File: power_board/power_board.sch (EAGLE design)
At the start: 25 parts, among them K2 RELAY-SPDT, Q1 600mA/40V, U2 ATSAMD21G-A

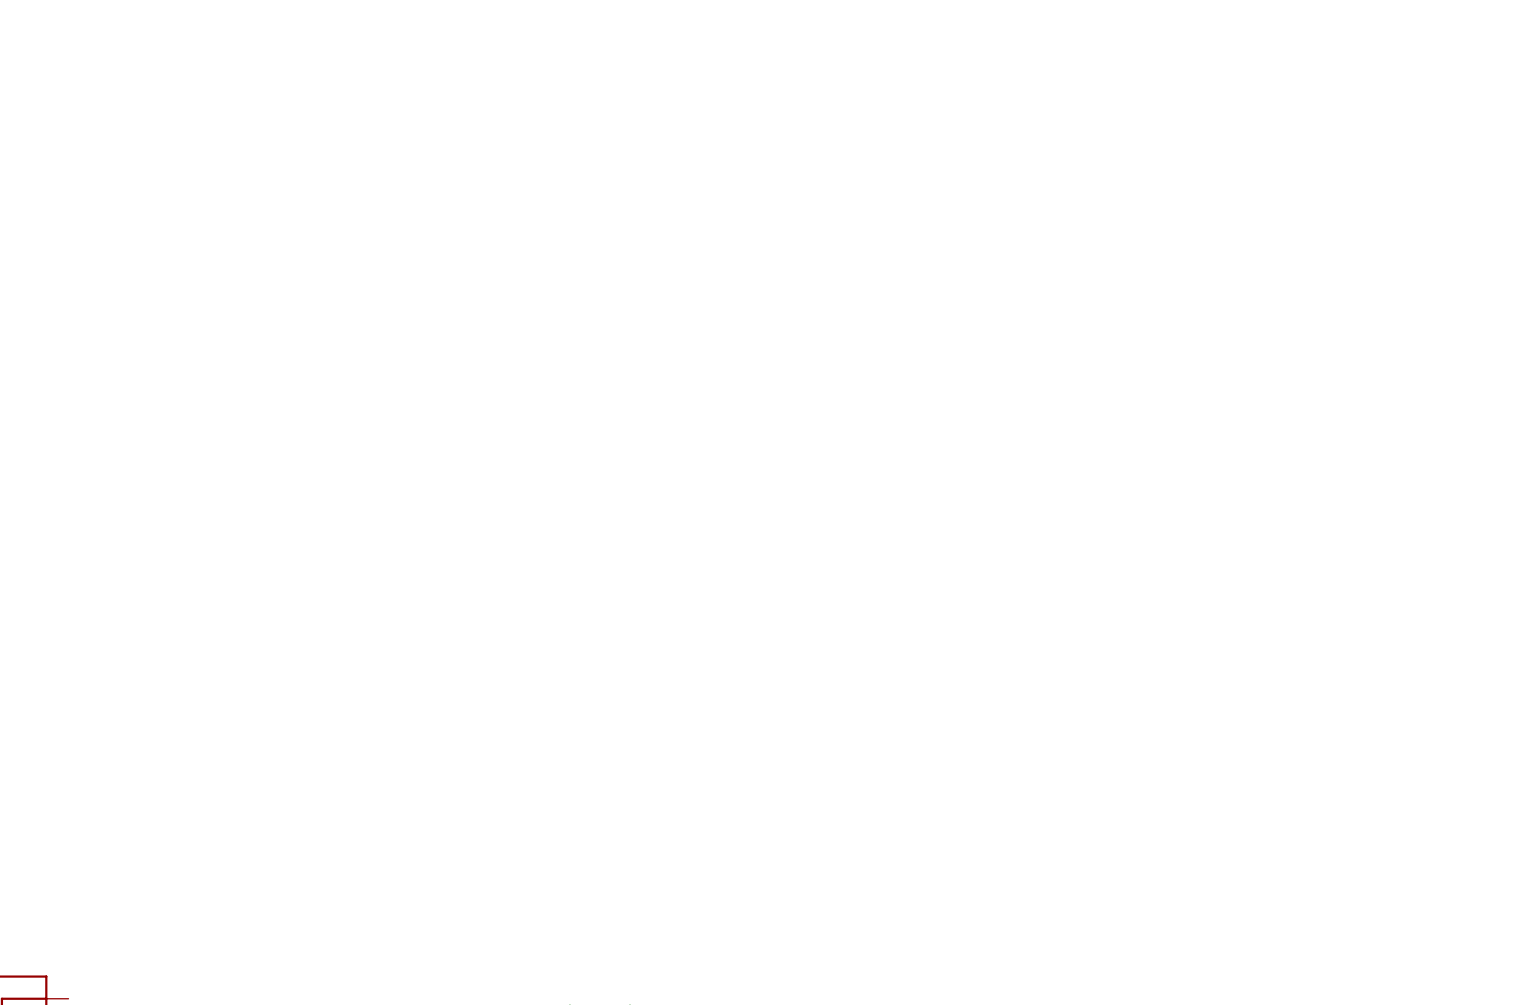
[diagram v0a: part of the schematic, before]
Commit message: Started adding NINA-B1
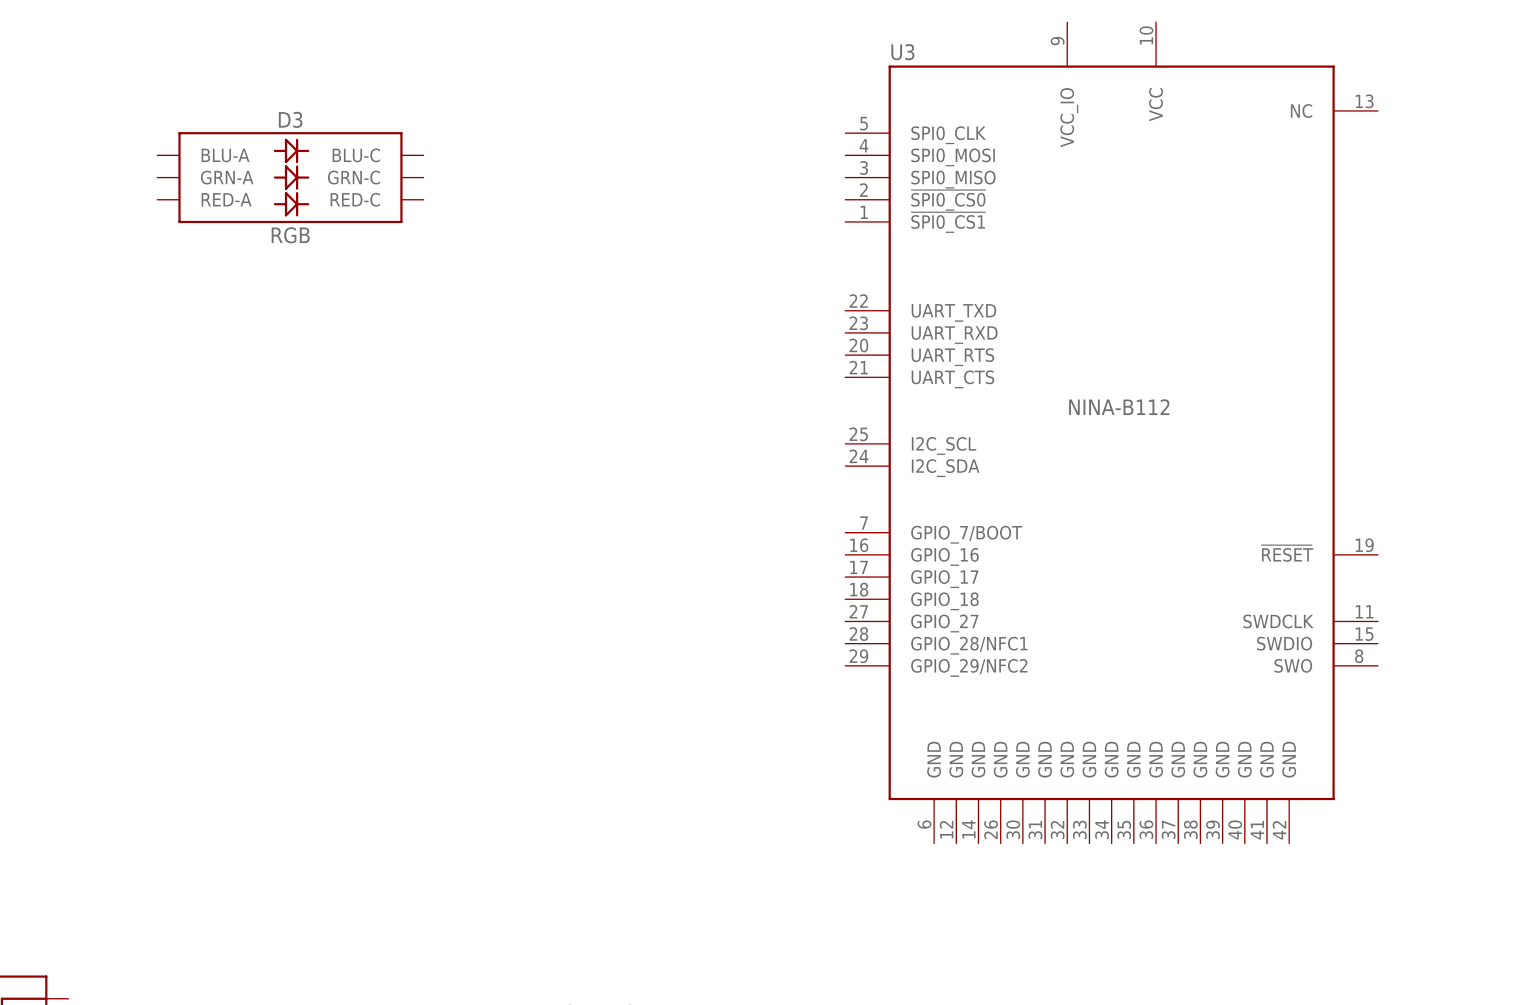
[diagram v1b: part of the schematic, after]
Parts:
- added D3: RGB, SparkFun-LED:LED-RGBPLCC-6
- added U3: NINA-B112, ubloxLib:NINA-B112
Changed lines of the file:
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@@
 <layer number="132" name="bAdjust" color="7" fill="1" visible="yes" active="yes"/>
 <layer number="144" name="Drill_legend" color="7" fill="1" visible="yes" active="yes"/>
+<layer number="145" name="DrillLegend_01-02" color="7" fill="1" visible="yes" active="yes"/>
+<layer number="146" name="DrillLegend_01-15" color="7" fill="1" visible="yes" active="yes"/>
+<layer number="147" name="DrillLegend_01-16" color="7" fill="1" visible="yes" active="yes"/>
+<layer number="148" name="DrillLegend_01-20" color="7" fill="1" visible="yes" active="yes"/>
+<layer number="149" name="DrillLegend_02-15" color="7" fill="1" visible="yes" active="yes"/>
 <layer number="150" name="Notes" color="7" fill="1" visible="yes" active="yes"/>
 <layer number="151" name="HeatSink" color="7" fill="1" visible="yes" active="yes"/>
@@
 <part name="C8" library="SparkFun-Capacitors" deviceset="0.1UF" device="-0603-25V-(+80/-20%)" value="0.1uF"/>
 <part name="U2" library="SparkFun-IC-Microcontroller" deviceset="ATSAMD21G" device="-A"/>
+<part name="U3" library="ubloxLib" deviceset="NINA-B112" device=""/>
+<part name="D3" library="SparkFun-LED" deviceset="LED-RGB" device="PLCC-6" value="RGB"/>
 </parts>
 <sheets>
@@
 <attribute name="VALUE" x="241.3" y="101.346" size="1.778" layer="96" align="top-left"/>
 </instance>
+<instance part="U3" gate="G$1" x="175.26" y="142.24" smashed="yes">
+<attribute name="VALUE" x="170.18" y="144.78" size="1.778" layer="96" align="top-left"/>
+<attribute name="NAME" x="149.86" y="185.42" size="1.778" layer="95" align="top-left"/>
+</instance>
+<instance part="D3" gate="G$1" x="81.28" y="170.18" smashed="yes">
+<attribute name="NAME" x="81.28" y="175.895" size="1.778" layer="95" font="vector" align="bottom-center"/>
+<attribute name="VALUE" x="81.28" y="164.465" size="1.778" layer="95" font="vector" align="top-center"/>
+</instance>
 </instances>

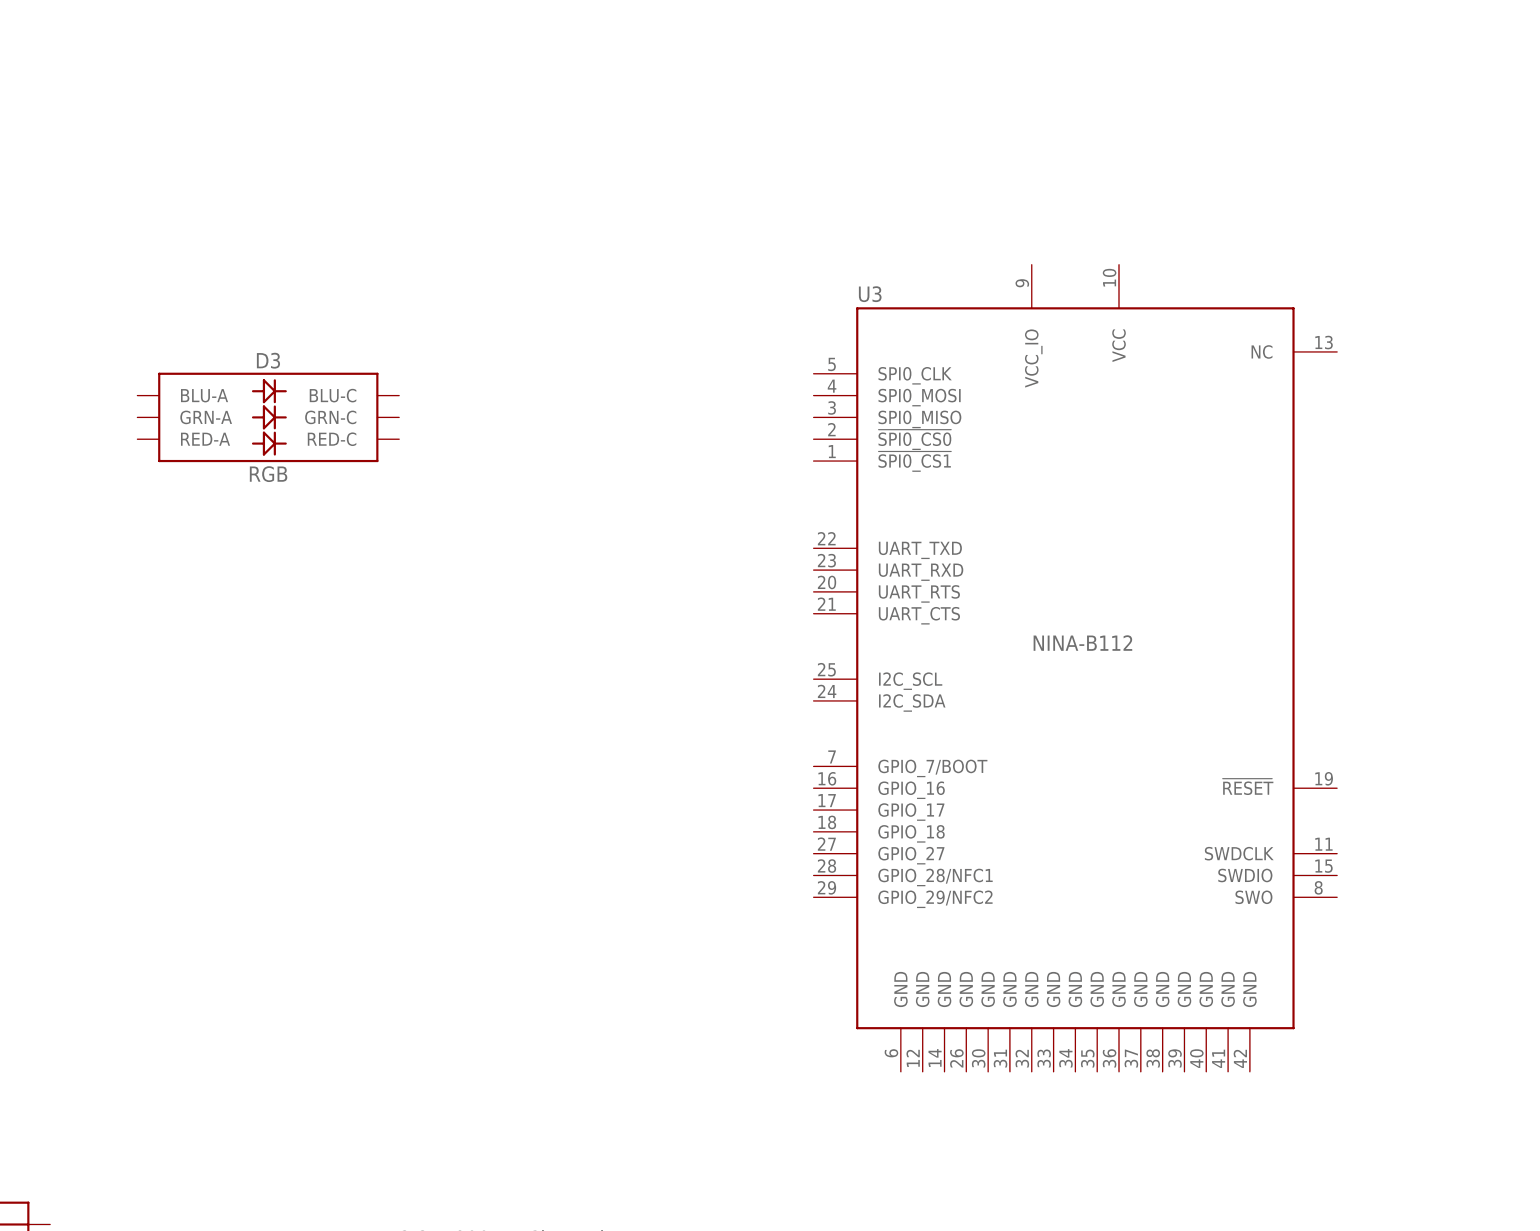
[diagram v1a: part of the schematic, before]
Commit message: Updated the schematics and added some more datasheets
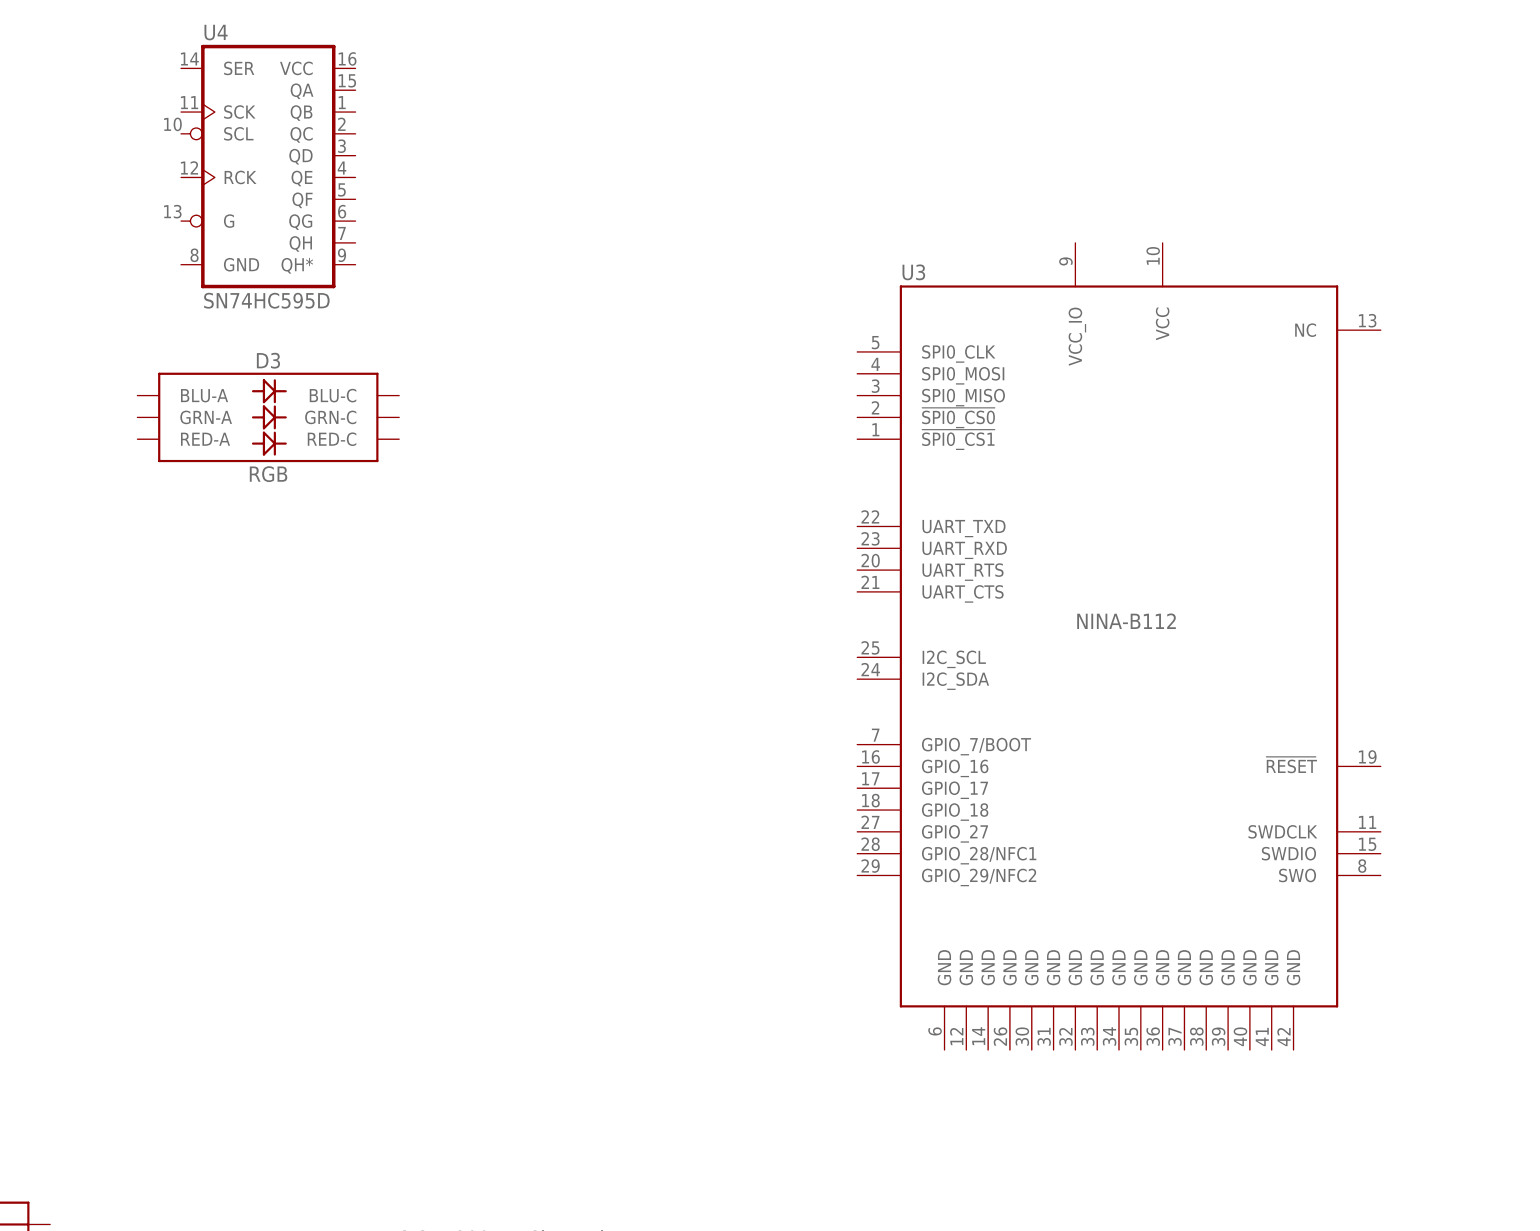
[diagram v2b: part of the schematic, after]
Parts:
- added U4: SN74HC595D, SparkFun-IC-Logic:74HC595D
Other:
- moved on the sheet: U3
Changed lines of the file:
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@@
 <part name="U3" library="ubloxLib" deviceset="NINA-B112" device=""/>
 <part name="D3" library="SparkFun-LED" deviceset="LED-RGB" device="PLCC-6" value="RGB"/>
+<part name="U4" library="SparkFun-IC-Logic" deviceset="74*595" device="D" technology="HC" value="SN74HC595D"/>
 </parts>
 <sheets>
@@
 <attribute name="VALUE" x="241.3" y="101.346" size="1.778" layer="96" align="top-left"/>
 </instance>
-<instance part="U3" gate="G$1" x="175.26" y="142.24" smashed="yes">
-<attribute name="VALUE" x="170.18" y="144.78" size="1.778" layer="96" align="top-left"/>
-<attribute name="NAME" x="149.86" y="185.42" size="1.778" layer="95" align="top-left"/>
+<instance part="U3" gate="G$1" x="180.34" y="144.78" smashed="yes">
+<attribute name="VALUE" x="175.26" y="147.32" size="1.778" layer="96" align="top-left"/>
+<attribute name="NAME" x="154.94" y="187.96" size="1.778" layer="95" align="top-left"/>
 </instance>
 <instance part="D3" gate="G$1" x="81.28" y="170.18" smashed="yes">
@@
 <attribute name="VALUE" x="81.28" y="164.465" size="1.778" layer="95" font="vector" align="top-center"/>
 </instance>
+<instance part="U4" gate="U1" x="78.74" y="200.66" smashed="yes">
+<attribute name="NAME" x="73.66" y="214.122" size="1.778" layer="95" font="vector"/>
+<attribute name="VALUE" x="73.66" y="182.88" size="1.778" layer="95" font="vector"/>
+</instance>
 </instances>

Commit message: Workedd on powerboard
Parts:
- added C10, C14, C18, C20, C22, C26, C28: 0.1uF, SparkFun-Capacitors:0.1UF-0603-25V-(+80/-20%)
- added C11, C12, C15, C16, C23, C24: 10uF, SparkFun-Capacitors:10UF-0603-6.3V-20%
- added C13, C17, C19, C21, C25, C27, C9: 1nF, SparkFun-Capacitors:1.0NF/1000PF-0603-50V-10%
- added D10, D12, D14, D16, D4, D6, D8: Red, SparkFun-LED:LED-RED0603-SMART
- added D11, D13, D15, D17, D5, D7, D9: 1A/23V/620mV, SparkFun-DiscreteSemi:DIODE-SCHOTTKY-BAT20J
- added J10, J4, J5, J6, J7, J8, J9: (no value), SparkFun-Connectors:CONN_023.5MM
- added JP2, JP3, JP4, JP5, JP6, JP7, JP8: JUMPER-SMT_2_NO_NO-SILK_ROUND, SparkFun-Jumpers:JUMPER-SMT_2_NO_NO-SILK_ROUND
- added K1, K3, K4, K5, K6, K7, K8: RELAY-SPDT, SparkFun-Electromechanical:RELAY-SPDT
- added Q2, Q3, Q4, Q5, Q6, Q7, Q8: 600mA/40V, SparkFun-DiscreteSemi:TRANS_NPN-MMBT2222AL
- added R10, R13, R14, R17, R18, R21, R22, R25, R26, R29, R30, R5, R6, R9: 330, SparkFun-Resistors:330OHM-0603-1/10W-1%
- added R11, R15, R19, R23, R27, R31, R7: 10, SparkFun-Resistors:10OHM-0603-1/10W-1%
- added R12, R16, R20, R24, R28, R32, R8: 4.7k, SparkFun-Resistors:4.7KOHM-0603-1/10W-1%
- added U$10, U$12, U$13, U$4, U$6, U$8, U$9: ACS712, SparkFun-Sensors:ACS712
- added U$11: 3.3V Voltage Regulator, SparkFun-IC-Power:V_REG_78XX-TO-220
- added U$5, U$7: 3.3V Voltage Regulator, SparkFun-IC-Power:V_REG_LD1117VXXLD1117-SMD
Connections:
- new net CTRL_2: R6.2
- new net CTRL_4: R18.2
- new net CTRL_5: R14.2
- new net CTRL_6: R26.2
- new net CTRL_7: R30.2
- new net CTRL_8: R10.2, R22.2
- new net CUR_2: C9.2, U$4.VOUT
- new net CUR_3: C13.2, U$6.VOUT
- new net CUR_5: C17.2, U$8.VOUT
- new net CUR_6: C25.2, U$12.VOUT
- new net CUR_7: C21.2, C27.2, U$10.VOUT, U$13.VOUT
- new net CUR_8: C19.2, U$9.VOUT
- new net N$10: D5.C, K1.COIL1, R7.1
- new net N$11: D4.C, R5.2
- new net N$12: Q2.B, R6.1
- new net N$13: C11.2, U$4.IP-@3, U$4.IP-@4, U$5.IN
- new net N$14: K1.NO, U$4.IP+@1, U$4.IP+@2
- new net N$15: JP2.2, R8.2, U$4.FILT
- new net N$16: C12.1, J4.1, U$5.OUT
- new net N$17: D7.A, K3.COIL2, Q3.C, R9.1
- new net N$18: D7.C, K3.COIL1, R11.1
- new net N$19: D6.C, R9.2
- new net N$20: Q3.B, R10.1
- new net N$21: C15.2, U$6.IP-@3, U$6.IP-@4, U$7.IN
- new net N$22: K3.NO, U$6.IP+@1, U$6.IP+@2
- new net N$23: JP3.2, R12.2, U$6.FILT
- new net N$24: C16.1, J5.1, U$7.OUT
- new net N$25: D9.A, K4.COIL2, Q4.C, R13.1
- new net N$26: J7.1, U$10.IP-@3, U$10.IP-@4
- new net N$27: D9.C, K4.COIL1, R15.1
- new net N$28: D8.C, R13.2
- new net N$29: Q4.B, R14.1
- new net N$30: K4.NO, U$8.IP+@1, U$8.IP+@2
- new net N$31: JP4.2, R16.2, U$8.FILT
- new net N$32: J6.1, U$8.IP-@3, U$8.IP-@4
- new net N$33: D11.A, K5.COIL2, Q5.C, R17.1
- new net N$34: D11.C, K5.COIL1, R19.1
- new net N$35: D10.C, R17.2
- new net N$36: Q5.B, R18.1
- new net N$37: D13.A, K6.COIL2, Q6.C, R21.1
- new net N$38: K5.NO, U$10.IP+@1, U$10.IP+@2
- new net N$39: JP5.2, R20.2, U$10.FILT
- new net N$40: D13.C, K6.COIL1, R23.1
- new net N$41: D12.C, R21.2
- new net N$42: Q6.B, R22.1
- new net N$43: C23.2, U$11.IN, U$9.IP-@3, U$9.IP-@4
- new net N$44: K6.NO, U$9.IP+@1, U$9.IP+@2
- new net N$45: JP6.2, R24.2, U$9.FILT
- new net N$46: C24.1, J8.1, U$11.OUT
- new net N$47: D15.A, K7.COIL2, Q7.C, R25.1
- new net N$48: D15.C, K7.COIL1, R27.1
- new net N$49: D14.C, R25.2
- new net N$50: Q7.B, R26.1
- new net N$51: K7.NO, U$12.IP+@1, U$12.IP+@2
- new net N$52: JP7.2, R28.2, U$12.FILT
- new net N$53: J9.1, U$12.IP-@3, U$12.IP-@4
- new net N$54: D17.A, K8.COIL2, Q8.C, R29.1
- new net N$55: D17.C, K8.COIL1, R31.1
- new net N$56: D16.C, R29.2
- new net N$57: Q8.B, R30.1
- new net N$58: K8.NO, U$13.IP+@1, U$13.IP+@2
- new net N$59: JP8.2, R32.2, U$13.FILT
- new net N$60: J10.1, U$13.IP-@3, U$13.IP-@4
- new net N$8: D5.A, K1.COIL2, Q2.C, R5.1
- net 12V: now also K1.MAIN, K3.MAIN, K4.MAIN, K5.MAIN, K6.MAIN, K7.MAIN, K8.MAIN
- net 3.3V: now also D10.A, D12.A, D14.A, D16.A, D4.A, D6.A, D8.A
- net 5V: now also C10.2, C14.2, C18.2, C20.2, C22.2, C26.2, C28.2, R11.2, R12.1, R15.2, R16.1, R19.2, R20.1, R23.2, R24.1, R27.2, R28.1, R31.2, R32.1, R7.2, R8.1, U$10.VCC, U$12.VCC, U$13.VCC, U$4.VCC, U$6.VCC, U$8.VCC, U$9.VCC
- net GND: now also C10.1, C11.1, C12.2, C13.1, C14.1, C15.1, C16.2, C17.1, C18.1, C19.1, C20.1, C21.1, C22.1, C23.1, C24.2, C25.1, C26.1, C27.1, C28.1, C9.1, J10.2, J4.2, J5.2, J6.2, J7.2, J8.2, J9.2, JP2.1, JP3.1, JP4.1, JP5.1, JP6.1, JP7.1, JP8.1, Q2.E, Q3.E, Q4.E, Q5.E, Q6.E, Q7.E, Q8.E, U$10.GND, U$11.GND, U$12.GND, U$13.GND, U$4.GND, U$5.GND, U$6.GND, U$7.GND, U$8.GND, U$9.GND, U3.GND@1, U3.GND@10, U3.GND@11, U3.GND@12, U3.GND@13, U3.GND@14, U3.GND@15, U3.GND@16, U3.GND@17, U3.GND@2, U3.GND@3, U3.GND@4, U3.GND@5, U3.GND@6, U3.GND@7, U3.GND@8, U3.GND@9
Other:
- note added: "12V 10A Channel"
- note added: "5 V 1.5A Channel"
- moved on the sheet: D3, U2, U3, U4
